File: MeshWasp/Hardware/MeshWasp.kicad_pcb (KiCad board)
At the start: 2 copper layers, 25.8 x 28.1 mm, 13 parts, among them SW1 RST, U1 CONN_MICROSD, U2 XBEE

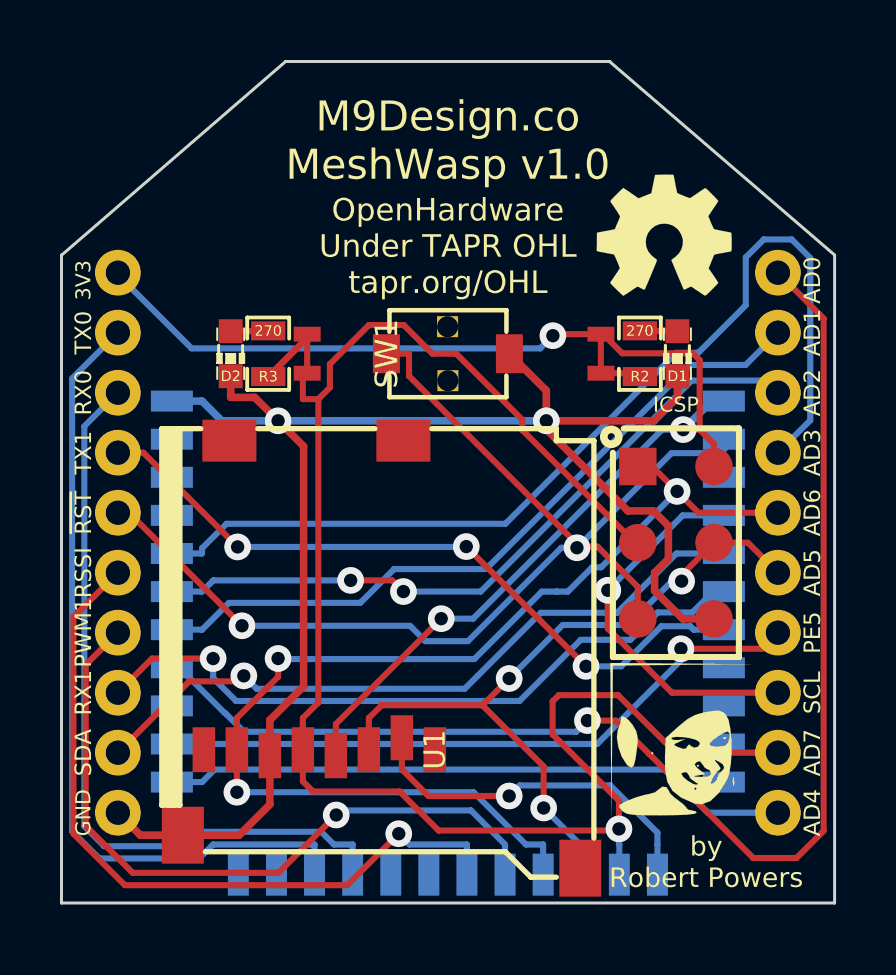
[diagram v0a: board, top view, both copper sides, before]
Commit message: Initial flip done.
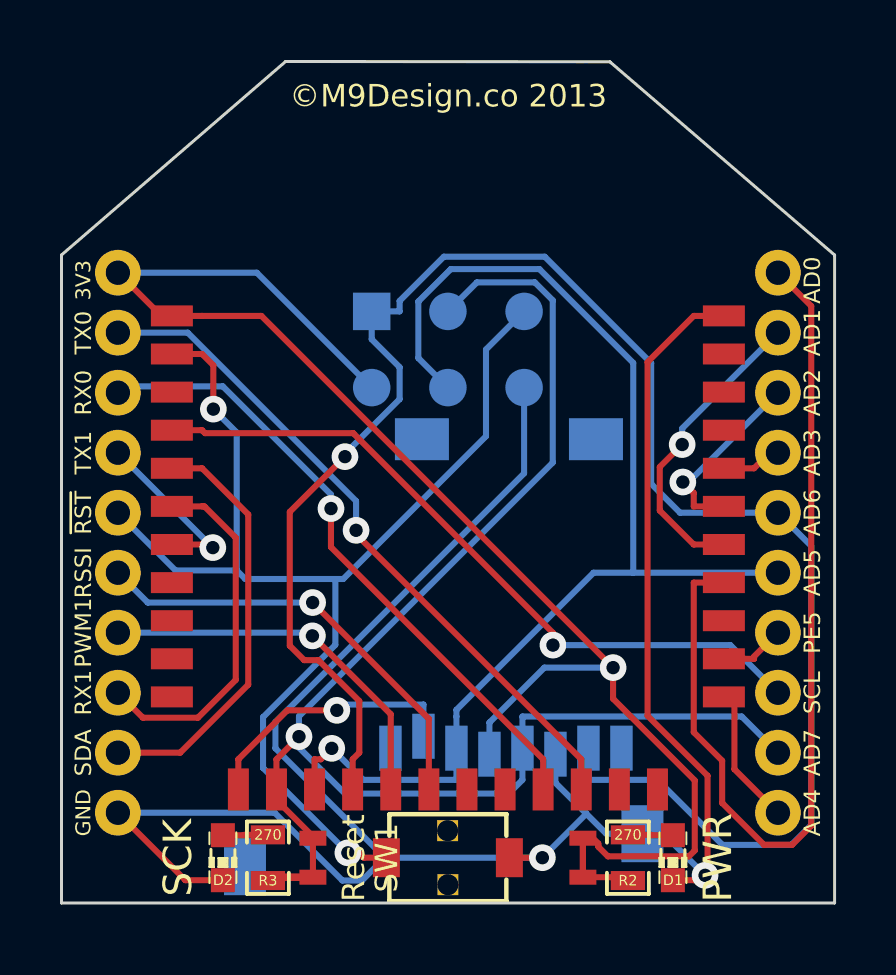
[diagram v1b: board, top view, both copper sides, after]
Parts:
- G1, G2, H2, U1: moved to B.Cu
- MT1: moved to F.Cu
- SJ1, SJ2: footprint _MT_MeshThing:_MT_SMTJumper -> _MW_MeshWasp:_MW_SMTJumper
- moved G2 19.0 mm to (144.0, 102.5)
- moved SJ1 16.8 mm to (154.5, 119.5)
- moved R2 16.8 mm to (156.0, 119.5)
- moved D2 16.8 mm to (142.5, 119.5)
- moved SJ2 16.8 mm to (145.5, 119.5), turned to 270 degrees
- moved D1 16.8 mm to (157.5, 119.5)
- moved R3 16.8 mm to (144.0, 119.5)
- moved SW1 16.8 mm to (150.0, 119.5)
- moved H2 9.96 mm to (150.0, 102.6), turned to 0 degrees
- moved MT1 2.84 mm to (150.0, 105.2), turned to 0 degrees
- moved U1 2.35 mm to (150.0, 112.9), turned to 0 degrees
- moved G1 0.80 mm to (157.3, 98.0)
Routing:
- net PF3-4: track 34.2 -> 1.67 mm
- net MISO: track 38.3 -> 60.4 mm, vias 3 -> 1
- net PE5: track 22.3 -> 1.86 mm, vias 1 -> 0
- net TX1: track 24.1 -> 6.23 mm, vias 3 -> 1
- net PF2: track 23.9 -> 6.72 mm, vias 2 -> 1
- net PE4: track 21.3 -> 4.46 mm
- net MOSI: track 25.0 -> 40.8 mm, vias 3 -> 1
- net PF1: track 24.7 -> 10.5 mm, vias 0 -> 1
- net PF0: track 44.6 -> 31.8 mm, vias 1 -> 0
- net SCL: track 13.1 -> 24.4 mm
- net PB4: track 24.2 -> 13.1 mm
- net SCK: track 57.2 -> 46.2 mm
- net RX1: track 23.5 -> 12.4 mm, vias 1 -> 0
- net PB5: track 25.4 -> 15.1 mm
- net GND: track 63.5 -> 73.7 mm
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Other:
- board text added: "PWR"
- board text added: "Reset"
- board text added: "SCK"

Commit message: Mostly silks and initial documentation.
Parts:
- U1: footprint _MT_MeshThing:_MT_microSD_3M_290805-A -> _MW_MeshWasp:_MW_microSD_3M_290805-A
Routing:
- net GND: track 73.7 -> 77.9 mm
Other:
- board text added: "MeshWasp v1.0 ©M9Design.co"
- board text added: "MeshWasp v1.0 ©M9Design.co 2013"
- board text removed: "M9Design.co MeshWasp v1.0"
- board text removed: "©M9Design.co 2013"

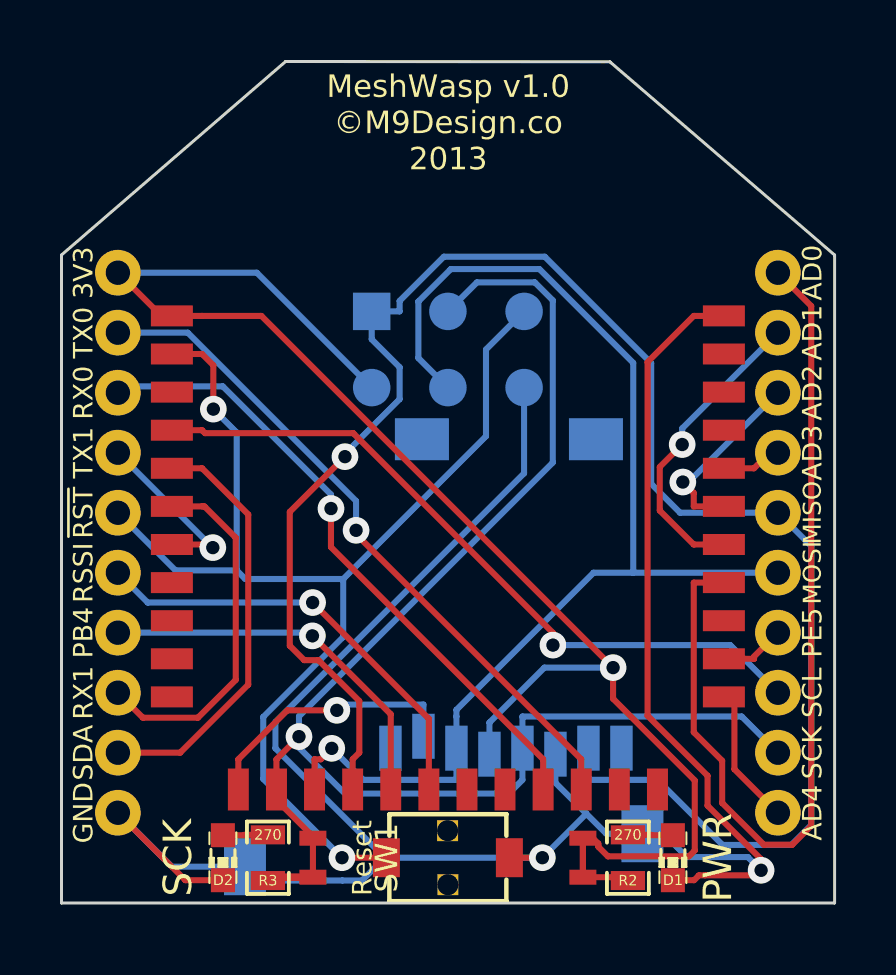
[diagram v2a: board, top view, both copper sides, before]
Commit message: Thicken pwr traces, mechanical relief on TH.
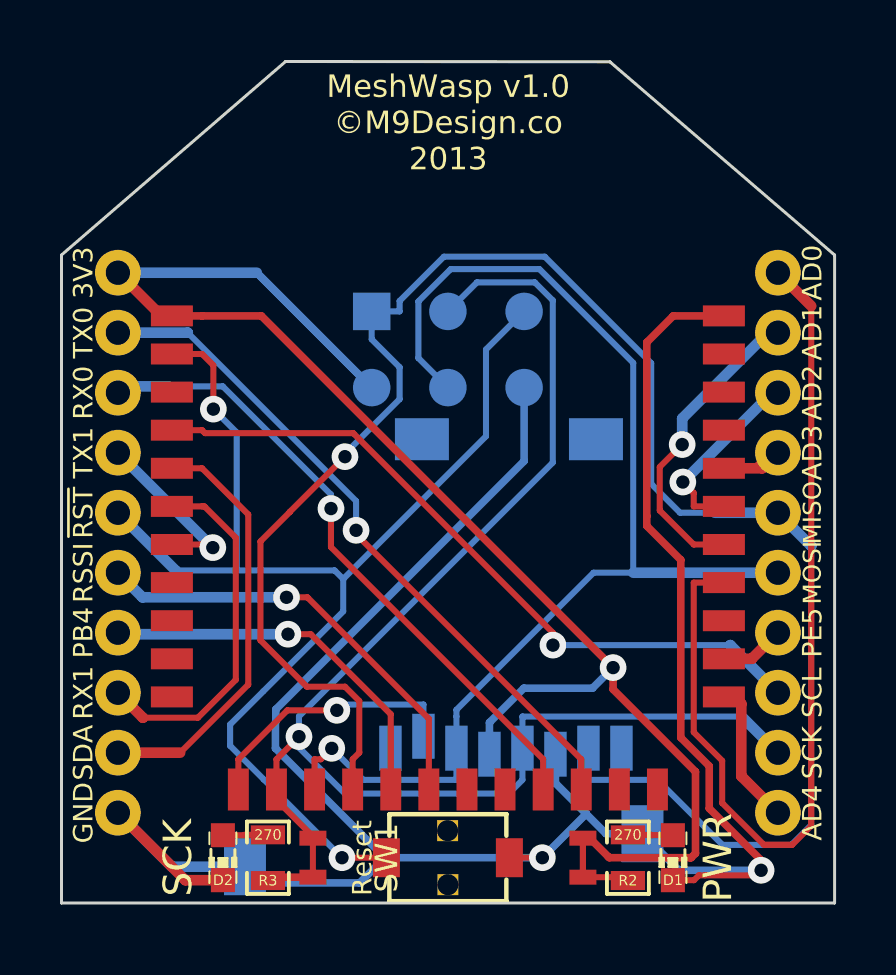
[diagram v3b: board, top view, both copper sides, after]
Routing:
- net GND: track 77.9 -> 90.0 mm
- net +3.3V: track 51.3 -> 62.8 mm
- net PB4: track 13.1 -> 18.8 mm
- net MISO: track 60.4 -> 65.4 mm
- net MOSI: track 40.8 -> 45.6 mm
- net PB5: track 15.1 -> 19.9 mm
- net TX1: track 6.23 -> 10.7 mm
- net Reset: track 41.9 -> 45.5 mm
- net TX0: track 23.3 -> 25.7 mm
- net SCL: track 24.4 -> 26.7 mm
- net SDA: track 14.5 -> 16.6 mm
- net PE5: track 1.86 -> 3.67 mm
- net RX0: track 21.8 -> 23.6 mm
- net SCK: track 46.2 -> 47.9 mm
- net PF3-4: track 1.67 -> 3.33 mm
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
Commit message: Logo work.
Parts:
- added VAL: M9Logo-flipped, _MW_LogoFlipped:M9Logo-flipped, B.Cu at (142.7, 97.8)
- moved G1 0.21 mm to (157.3, 97.8)

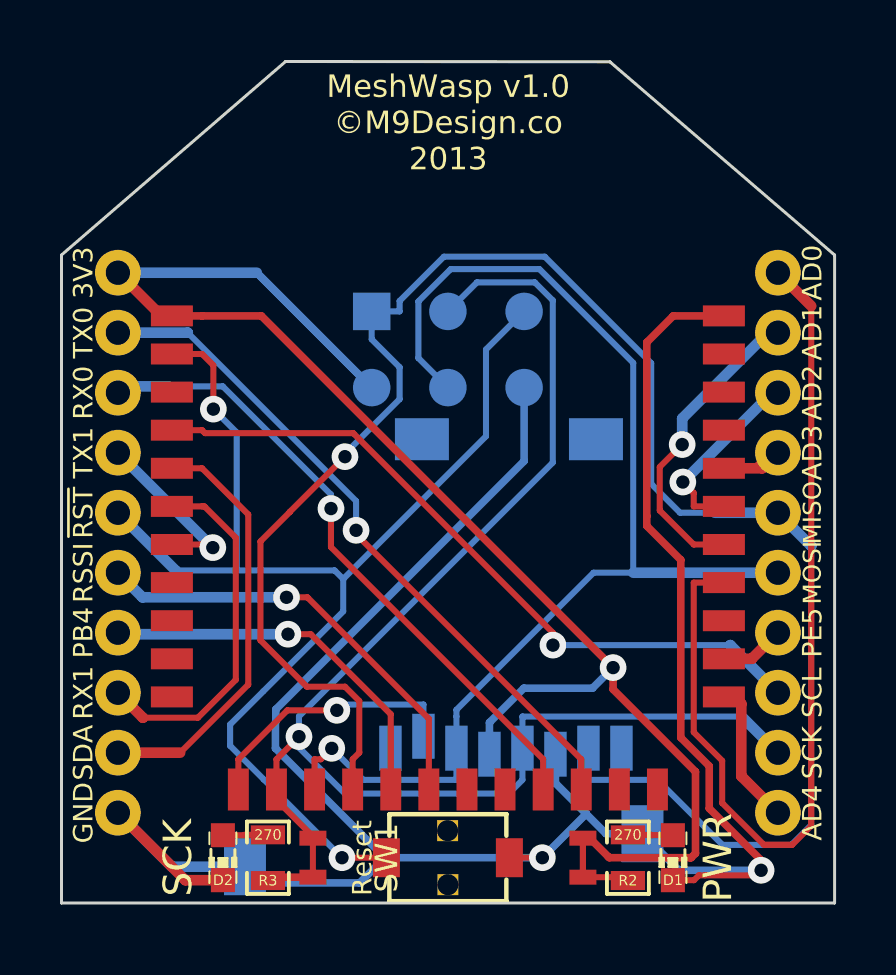
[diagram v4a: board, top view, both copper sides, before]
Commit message: ICSP keepout recognized on MW. Silks, gerbers.
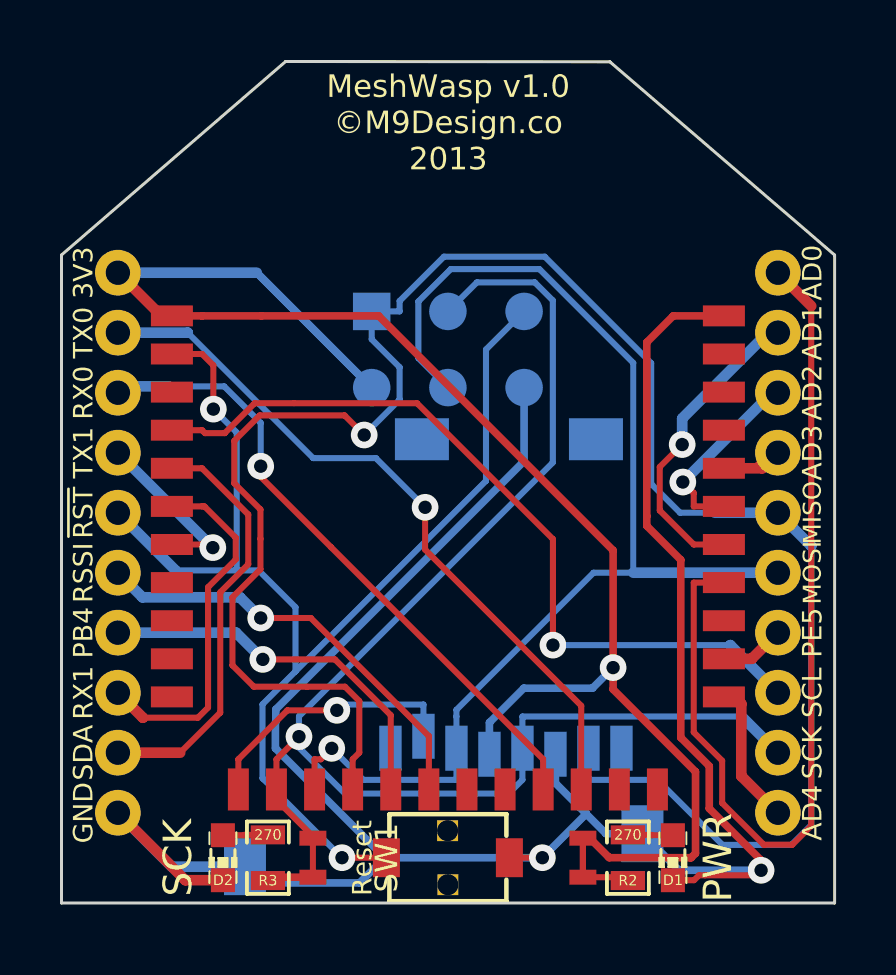
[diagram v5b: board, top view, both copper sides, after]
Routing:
- net MISO: track 65.4 -> 70.9 mm
- net PB4: track 18.8 -> 14.3 mm
- net PB5: track 19.9 -> 15.7 mm
- net SCL: track 26.7 -> 29.3 mm
- net +3.3V: track 62.8 -> 65.0 mm
- net TX0: track 25.7 -> 26.9 mm

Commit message: Minor silks & logo work.
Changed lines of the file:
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@@
     (links 44)
     (no_connects 0)
-    (area 137.069999 92.909999 162.940001 121.060001)
+    (area 135.5699 92.646799 162.940001 121.228201)
     (thickness 1.6)
     (drawings 13)
@@
     (18 B.Paste user)
     (19 F.Paste user)
-    (20 B.SilkS user hide)
+    (20 B.SilkS user)
     (21 F.SilkS user)
-    (22 B.Mask user hide)
-    (23 F.Mask user hide)
+    (22 B.Mask user)
+    (23 F.Mask user)
     (24 Dwgs.User user)
     (25 Cmts.User user)
-    (26 Eco1.User user)
+    (26 Eco1.User user hide)
     (27 Eco2.User user)
     (28 Edge.Cuts user)
@@
     (effects (font (size 0.75 0.75) (thickness 0.1875)) (justify mirror))
   )
-  (gr_text "MeshWasp v1.0\n©M9Design.co \n2013" (at 150.01 95) (layer F.SilkS)
-    (effects (font (size 0.75 0.75) (thickness 0.1875)))
+  (gr_text "MeshWasp v1.0\n©M9Design.co \n2013" (at 150.01 96) (layer F.SilkS)
+    (effects (font (size 1 1) (thickness 0.1875)))
   )
   (gr_text "by\nRobert\nPowers" (at 156 103) (layer B.SilkS)
